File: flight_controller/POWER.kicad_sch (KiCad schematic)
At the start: 3 parts, among them J10 A2012WV-S-9P

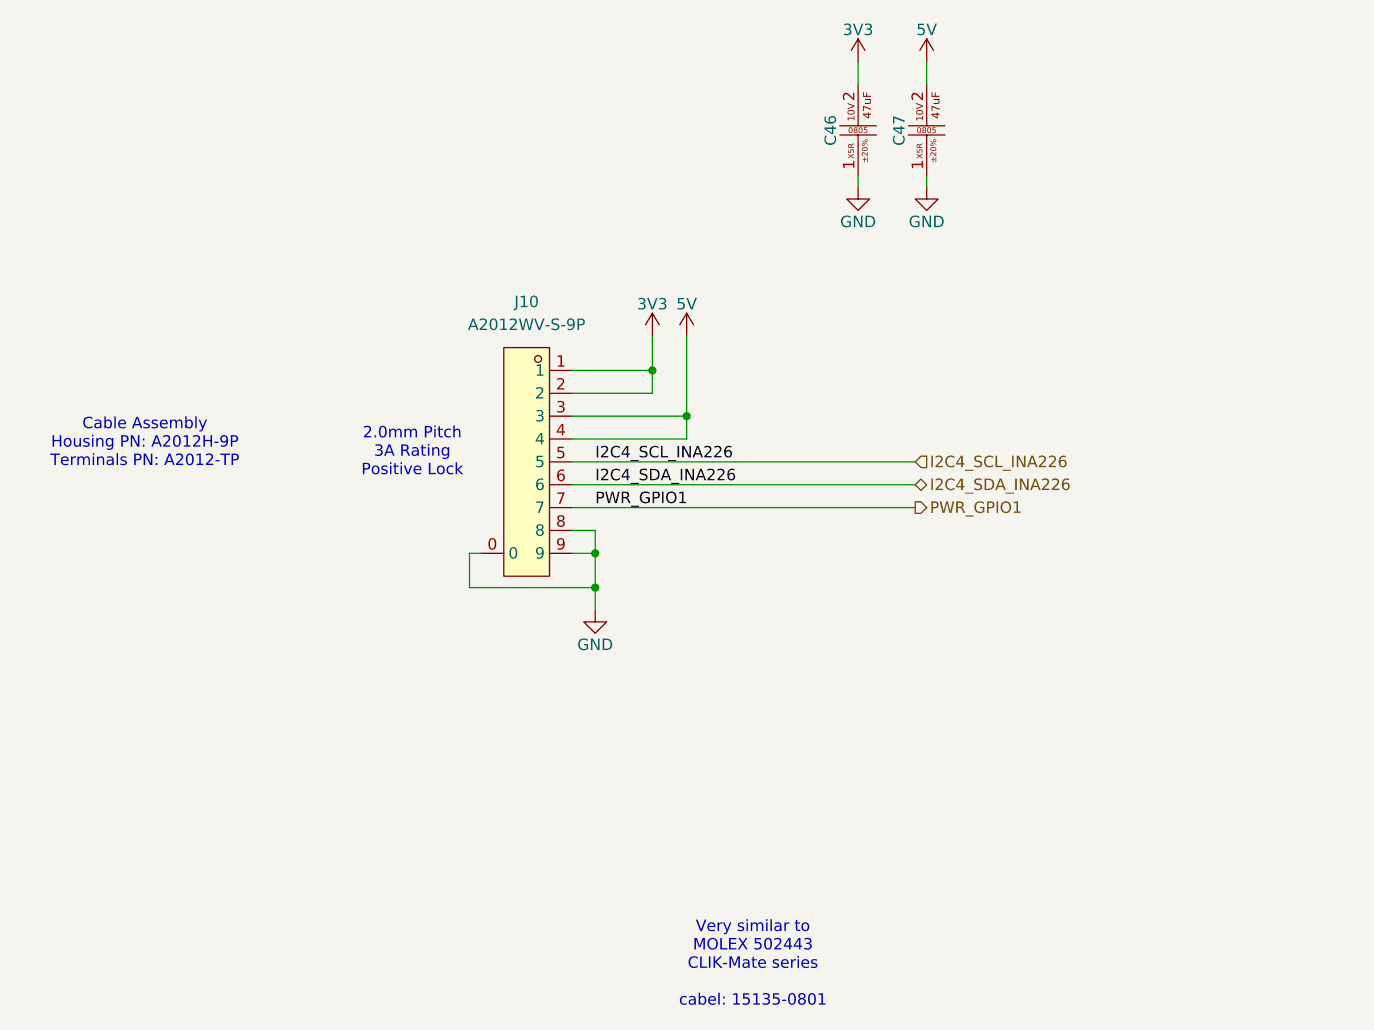
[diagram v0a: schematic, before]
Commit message: Updated power and usb connectors and netlist check
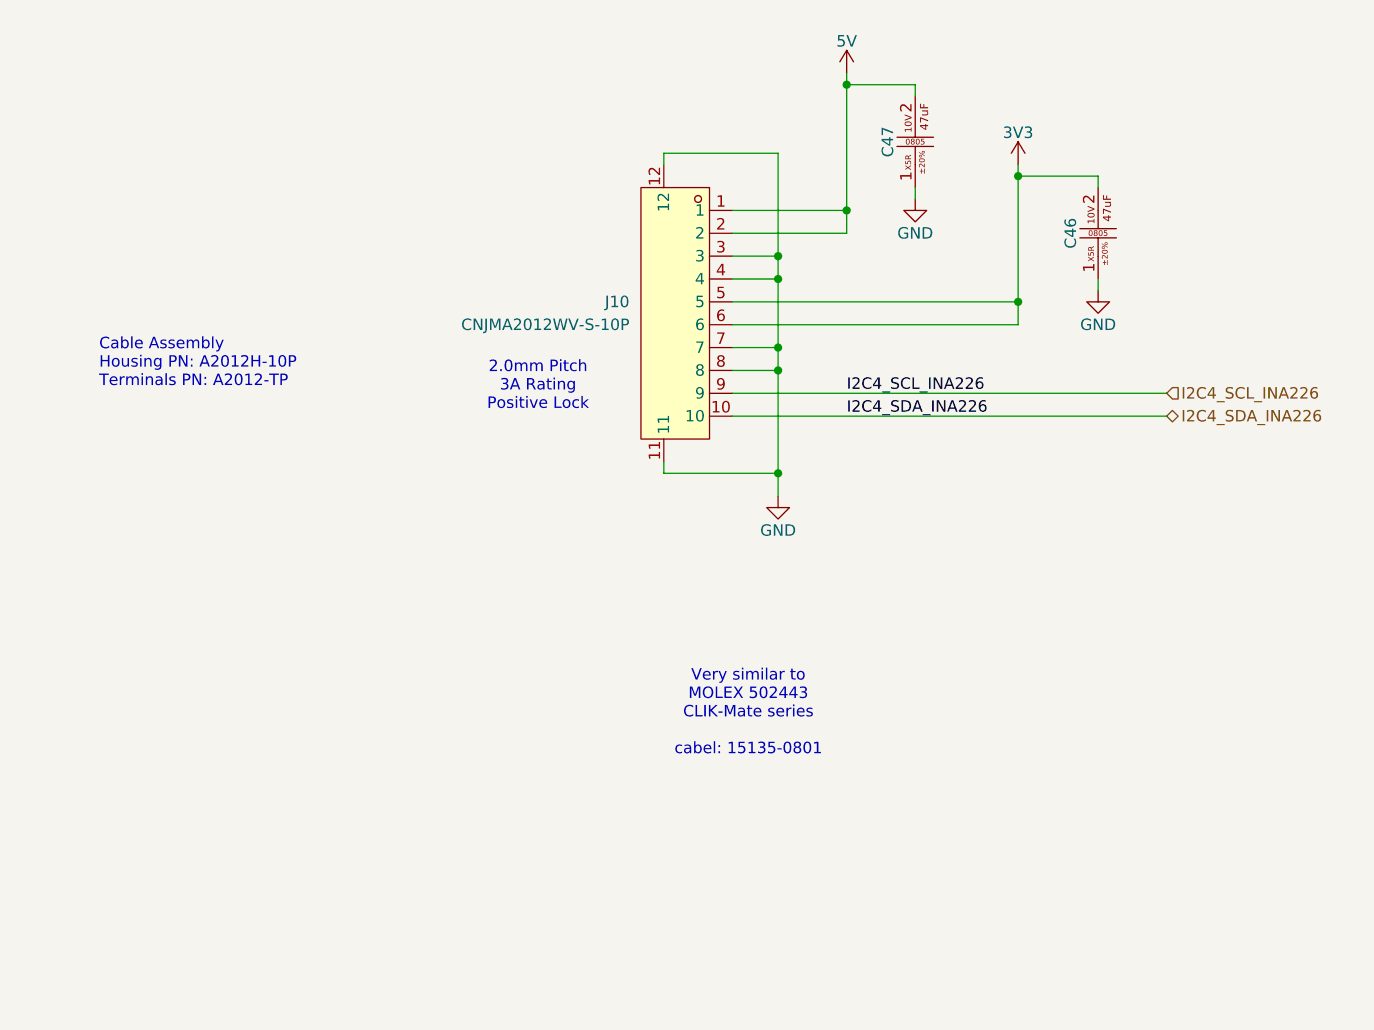
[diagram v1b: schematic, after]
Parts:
- removed J10: A2012WV-S-9P, easyeda2kicad:CONN-SMD_A2012WV-S-9P, symbol lampelKicadLIB:A2012WV-S-9P
- added J10: CNJMA2012WV-S-10P, easyeda2kicad:CONN-SMD_10P-P1.25_CNJM_CNJMA2012WV-S-10P, symbol lampelKicadLIB:CNJMA2012WV-S-10P
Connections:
- net 3V3: now also J10.5, J10.6
- net 5V: now also J10.1, J10.2
- net GND: now also J10.11, J10.12, J10.3, J10.4, J10.7, J10.8
- net I2C4_SCL_INA226: now also J10.9
- net I2C4_SDA_INA226: now also J10.10
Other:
- note added: "Cable Assembly Housing PN: A2012H-10P Terminals PN: A2012-TP"
- note removed: "Cable Assembly Housing PN: A2012H-9P Terminals PN: A2012-TP"
- moved on the sheet: C46, C47
